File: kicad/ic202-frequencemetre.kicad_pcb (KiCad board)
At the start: 2 copper layers, 80 x 50 mm, 49 parts, among them J1 +12V IN (4 pins: 2x+12V, 2x G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, J2 RF IN, J4 LCD, Q1 2SC5551AE-TD-E, U1 AMS1117-5.0, U2 AMS1117 (ADJ), U3 MB506

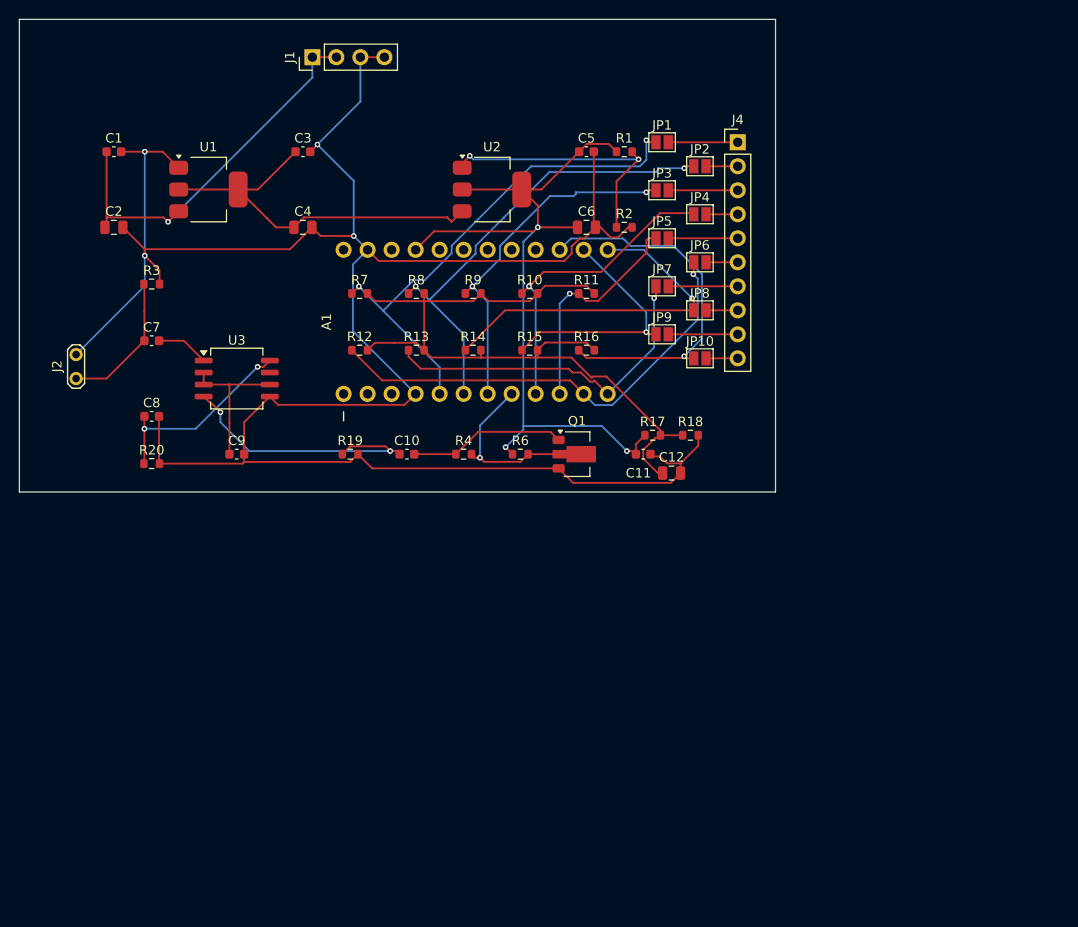
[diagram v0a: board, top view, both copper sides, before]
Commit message: routage refait par GPT-6 avec le prompt: "refais le placement complet du pcb et ensuite routage, tiens compte des boucles a minimiser comme l'indique les attributs Placement des composants. Fais un circuit rectangulaire compact plus petit que le pourtour du pcb actuel, place le connecteur J4 a droite et au milieu du pcb, les broches du arduino-pro mini paralleles aux broches de J4 afin de facilite certaines liaisons qui seront en ligne presque droites. Tu peux placer des composants sous le arduino-pro entre les broches, tu peux placer des composants des 2 cotés, mets le connecteur J2 pres du board gauche en bas et le connecteur alimentation pres du bord haut vers la gauche parallele au bord haut " passage a BigPickle pour lancement de l'autoroutage et correction des erreurs DRC sur le silkscreen
Corrige les chevauchements silkscreen des champs Reference (DRC 0 violation)

Deplace les textes Reference de R1, R15, R16, C1 et J1 hors des
lignes/pads silkscreen voisins (cadre du connecteur J1, range de
resistances au pas 2,54 mm). DRC final : 0 erreur, 0 warning.

Ignore en plus les rapports DRC (.rpt) et l'historique local de
recuperation KiCad (kicad/.history/).
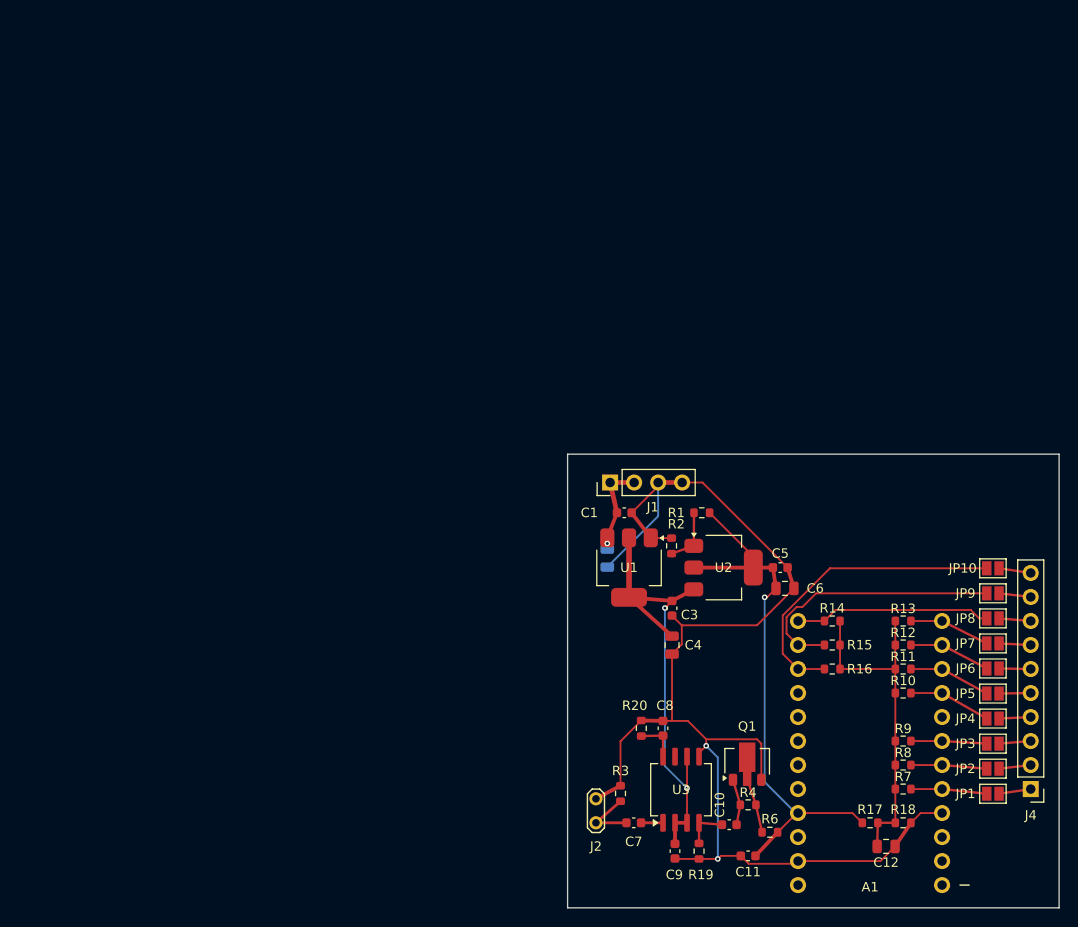
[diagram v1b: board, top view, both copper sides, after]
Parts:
- C2: moved to B.Cu
- moved R7 77.8 mm to (158.0, 116.4), turned to 180 degrees
- moved JP1 77.3 mm to (167.5, 116.9)
- moved J4 75.1 mm to (171.5, 116.4), turned to 180 degrees
- moved R3 73.2 mm to (128.1, 116.9), turned to 90 degrees
- moved J2 72.3 mm to (125.5, 120.0)
- moved C7 72.1 mm to (129.5, 120.0)
- moved R8 71.7 mm to (158.0, 113.9), turned to 180 degrees
- moved JP2 70.9 mm to (167.5, 114.3)
- moved JP3 68.2 mm to (167.5, 111.6)
- moved C1 66.1 mm to (128.5, 87.2)
- moved R9 65.7 mm to (158.0, 111.3), turned to 180 degrees
- moved R12 65.4 mm to (158.0, 101.2), turned to 180 degrees
- moved U3 64.0 mm to (134.5, 116.5), turned to 90 degrees
- moved A1 63.6 mm to (154.5, 113.9), turned to 180 degrees
- moved C8 63.4 mm to (132.6, 110.0), turned to 90 degrees
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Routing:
- net GND: track 243.3 -> 140.5 mm, vias 4 -> 2
- net VLCD_MID: track 84.6 -> 36.6 mm
- net LCD_COM1: track 54.0 -> 8.05 mm, vias 2 -> 0
- net LCD_COM2: track 49.0 -> 8.04 mm, vias 2 -> 0
- net LCD_SEG2: track 49.0 -> 8.64 mm, vias 1 -> 0
- net +12V: track 42.6 -> 9.86 mm
- net LCD_COM3: track 37.7 -> 8.03 mm, vias 2 -> 0
- net LCD_SEG3: track 37.0 -> 8.59 mm, vias 1 -> 0
- net MB506_OUT: track 29.5 -> 4.60 mm, vias 2 -> 0
- net LCD_COM4: track 33.4 -> 8.74 mm, vias 1 -> 0
- net U2_ADJ: track 28.8 -> 5.99 mm, vias 2 -> 0
- net +3V: track 82.7 -> 60.1 mm, vias 3 -> 1
- net LCD_SEG4: track 38.3 -> 20.8 mm, vias 1 -> 0
- net MB506_NIN: track 21.3 -> 4.52 mm, vias 2 -> 0
- net LCD_SEG1: track 24.0 -> 8.69 mm, vias 1 -> 0
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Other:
- board size 80 x 50 mm -> 52 x 48 mm
